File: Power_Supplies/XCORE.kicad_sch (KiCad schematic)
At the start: 11 parts, among them J22 FTSH-110-01-F-DV-K XTAG HEADER, U10 XU316-1024-TQ128-I24, U11 W25Q64JVSSIQ (FLASH MEMORY), X1 FA-238 24.0000MB-C0 (CRYSTAL)

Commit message: Added 3.3V/1.8V LDO, clock IC
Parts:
- removed C196, C197: 100N, Capacitor_SMD:C_0402_1005Metric, symbol Device:C
- removed J22: FTSH-110-01-F-DV-K XTAG HEADER, CON20_2X10_DUK_FTSH_SAI, symbol SDLibrary:FTSH-110-01-F-DV-K
- removed R174: 0, symbol Device:R
- added R45: 33, Resistor_SMD:R_0805_2012Metric, symbol Device:R
- added U31: Si5351A-B-GT, Package_SO:MSOP-10_3x3mm_P0.5mm, symbol Oscillator:Si5351A-B-GT
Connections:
- net 3.3V: now also U31.1 (VDD), U31.7 (VDDO); no longer U10.61 (USB_VDD33)
- net AGND: now also U31.8 (GND)
- removed net 0.9V: U10.14 (VDD), U10.41 (PLL_AVDD), U10.5 (VDD)
- removed net 1.8V: U10.35 (VDDIOB18), U10.56 (VDDIOB18), U10.62 (USB_VDD18)
- net XIN: no longer names the net of C100.2, R28.1, U10.34 (XIN)
- net XIN: no longer X1.1
- net XOUT: no longer names the net of C101.1, R28.2, U10.33 (XOUT)
- net XOUT: no longer X1.3
- new net: R45.1, U31.10 (CLK0)
- new net: U31.2 (XA), X1.1
- new net: U31.3 (XB), X1.3
- new net BCK: U31.6 (CLK2)
- new net LRCK: U31.9 (CLK1)
- new net MCLK: R45.2
- new net SCL: U31.4 (SCL)
- new net SDA: U31.5 (SDA)
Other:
- note added: "Device address = 0x60"
- note removed: "What are these for? (The XLs)"
- company: Joshua Yu -> Michael Meyers
- moved on the sheet: C100, C101, R28, R29, U10A, U10B, U11

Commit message: big things are coming...
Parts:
- X1: footprint FA-238_EPS -> SamacSys_Parts:FA-238_EPS
- renumbered C100 to C49, C101 to C50, R29 to R34, R45 to R35, R28 to R36, U10 to U12, U31 to U13, U11 to U14
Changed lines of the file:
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@@
 		(dnp no)
 		(fields_autoplaced yes)
-		(property "Reference" "C100"
+		(property "Reference" "C49"
 			(at 132.08 135.8899 0)
 			(effects
@@
 			(project ""
 				(path "/5266cf9e-da90-4c53-80fd-cf3dbed42632/4ac374da-48c1-45fc-82eb-58af98bfd6f4"
-					(reference "C100")
+					(reference "C49")
 					(unit 1)
 				)
@@
 		(dnp no)
 		(fields_autoplaced yes)
-		(property "Reference" "#PWR062"
+		(property "Reference" "#PWR047"
 			(at 76.2 175.26 0)
 			(effects
@@
 			(project "Power_Supplies"
 				(path "/5266cf9e-da90-4c53-80fd-cf3dbed42632/4ac374da-48c1-45fc-82eb-58af98bfd6f4"
-					(reference "#PWR062")
+					(reference "#PWR047")
 					(unit 1)
 				)
@@
 		(dnp no)
 		(fields_autoplaced yes)
-		(property "Reference" "#PWR0101"
+		(property "Reference" "#PWR049"
 			(at 114.3 48.26 0)
 			(effects
@@
 			(project "Power_Supplies"
 				(path "/5266cf9e-da90-4c53-80fd-cf3dbed42632/4ac374da-48c1-45fc-82eb-58af98bfd6f4"
-					(reference "#PWR0101")
+					(reference "#PWR049")
 					(unit 1)
 				)
@@
 		(dnp no)
 		(fields_autoplaced yes)
-		(property "Reference" "U10"
+		(property "Reference" "U12"
 			(at 217.17 52.07 0)
 			(effects
@@
 			(project ""
 				(path "/5266cf9e-da90-4c53-80fd-cf3dbed42632/4ac374da-48c1-45fc-82eb-58af98bfd6f4"
-					(reference "U10")
+					(reference "U12")
 					(unit 2)
 				)
@@
 		(dnp no)
 		(fields_autoplaced yes)
-		(property "Reference" "R29"
+		(property "Reference" "R34"
 			(at 102.87 17.78 90)
 			(effects
@@
 			(project ""
 				(path "/5266cf9e-da90-4c53-80fd-cf3dbed42632/4ac374da-48c1-45fc-82eb-58af98bfd6f4"
-					(reference "R29")
+					(reference "R34")
 					(unit 1)
 				)
@@
 		(dnp no)
 		(fields_autoplaced yes)
-		(property "Reference" "U31"
+		(property "Reference" "U13"
 			(at 101.2541 184.15 0)
 			(effects
@@
 			(project "Power_Supplies"
 				(path "/5266cf9e-da90-4c53-80fd-cf3dbed42632/4ac374da-48c1-45fc-82eb-58af98bfd6f4"
-					(reference "U31")
+					(reference "U13")
 					(unit 1)
 				)
@@
 		(dnp no)
 		(fields_autoplaced yes)
-		(property "Reference" "U11"
+		(property "Reference" "U14"
 			(at 154.94 21.59 0)
 			(effects
@@
 			(project ""
 				(path "/5266cf9e-da90-4c53-80fd-cf3dbed42632/4ac374da-48c1-45fc-82eb-58af98bfd6f4"
-					(reference "U11")
+					(reference "U14")
 					(unit 1)
 				)
@@
 		(dnp no)
 		(fields_autoplaced yes)
-		(property "Reference" "#PWR061"
+		(property "Reference" "#PWR046"
 			(at 41.91 177.8 0)
 			(effects
@@
 			(project "Power_Supplies"
 				(path "/5266cf9e-da90-4c53-80fd-cf3dbed42632/4ac374da-48c1-45fc-82eb-58af98bfd6f4"
-					(reference "#PWR061")
+					(reference "#PWR046")
 					(unit 1)
 				)
@@
 		(dnp no)
 		(fields_autoplaced yes)
-		(property "Reference" "U10"
+		(property "Reference" "U12"
 			(at 88.9 52.07 0)
 			(effects
@@
 			(project ""
 				(path "/5266cf9e-da90-4c53-80fd-cf3dbed42632/4ac374da-48c1-45fc-82eb-58af98bfd6f4"
-					(reference "U10")
+					(reference "U12")
 					(unit 1)
 				)
@@
 		(dnp no)
 		(fields_autoplaced yes)
-		(property "Reference" "#PWR0103"
+		(property "Reference" "#PWR048"
 			(at 99.06 190.5 0)
 			(effects
@@
 			(project "Power_Supplies"
 				(path "/5266cf9e-da90-4c53-80fd-cf3dbed42632/4ac374da-48c1-45fc-82eb-58af98bfd6f4"
-					(reference "#PWR0103")
+					(reference "#PWR048")
 					(unit 1)
 				)
@@
 		(dnp no)
 		(fields_autoplaced yes)
-		(property "Reference" "R45"
+		(property "Reference" "R35"
 			(at 118.11 160.02 90)
 			(effects
@@
 			(project "Power_Supplies"
 				(path "/5266cf9e-da90-4c53-80fd-cf3dbed42632/4ac374da-48c1-45fc-82eb-58af98bfd6f4"
-					(reference "R45")
+					(reference "R35")
 					(unit 1)
 				)
@@
 		(dnp no)
 		(fields_autoplaced yes)
-		(property "Reference" "#PWR0105"
+		(property "Reference" "#PWR050"
 			(at 128.27 127 0)
 			(effects
@@
 			(project ""
 				(path "/5266cf9e-da90-4c53-80fd-cf3dbed42632/4ac374da-48c1-45fc-82eb-58af98bfd6f4"
-					(reference "#PWR0105")
+					(reference "#PWR050")
 					(unit 1)
 				)
@@
 		(dnp no)
 		(fields_autoplaced yes)
-		(property "Reference" "R28"
+		(property "Reference" "R36"
 			(at 128.27 144.7799 0)
 			(effects
@@
 			(project ""
 				(path "/5266cf9e-da90-4c53-80fd-cf3dbed42632/4ac374da-48c1-45fc-82eb-58af98bfd6f4"
-					(reference "R28")
+					(reference "R36")
 					(unit 1)
 				)
@@
 			)
 		)
-		(property "Footprint" "FA-238_EPS"
+		(property "Footprint" "SamacSys_Parts:FA-238_EPS"
 			(at 46.99 167.64 0)
 			(effects
@@
 		(dnp no)
 		(fields_autoplaced yes)
-		(property "Reference" "#PWR0102"
+		(property "Reference" "#PWR051"
 			(at 165.1 165.1 0)
 			(effects
@@
 			(project "Power_Supplies"
 				(path "/5266cf9e-da90-4c53-80fd-cf3dbed42632/4ac374da-48c1-45fc-82eb-58af98bfd6f4"
-					(reference "#PWR0102")
+					(reference "#PWR051")
 					(unit 1)
 				)
@@
 		(dnp no)
 		(fields_autoplaced yes)
-		(property "Reference" "C101"
+		(property "Reference" "C50"
 			(at 168.91 153.6699 0)
 			(effects
@@
 			(project "Power_Supplies"
 				(path "/5266cf9e-da90-4c53-80fd-cf3dbed42632/4ac374da-48c1-45fc-82eb-58af98bfd6f4"
-					(reference "C101")
+					(reference "C50")
 					(unit 1)
 				)

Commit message: More XCORE PCB updates
Finished XTAG header, reinstated clock, worked on power pins
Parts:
- added C202, C203, C204, C205, C207, C208, C209, C210, C211, C212, C213, C214, C215, C216, C217, C218: 100nF, Capacitor_SMD:C_0402_1005Metric, symbol Device:C
- added C206: 2.2uF, Capacitor_SMD:C_0402_1005Metric, symbol Device:C
- added J8: FTSH-110-01-F-DV-K, CON20_2X10_DUK_FTSH_SAI, symbol SDLibrary:FTSH-110-01-F-DV-K
- added R164: 0, Resistor_SMD:R_0805_2012Metric, symbol Device:R
- added R165, R166: 43, Resistor_SMD:R_0805_2012Metric, symbol Device:R
- added X2: FA-238 24.0000MB-C0, FA-238_EPS, symbol SDLibrary:FA-238_24.0000MB-C0
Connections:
- net 3.3V: now also C203.1, J8.11
- net AGND: now also U12.129 (GND), U12.30 (GND), C202.2, C203.2, C204.2, C205.2, C206.2, C207.2, C208.2, C209.2, C210.2, C211.2, C212.2, C213.2, C214.2, C215.2, C216.2, C217.2, C218.2, J8.13, J8.15, J8.17, J8.19, J8.3, J8.5, J8.7, J8.9, X2.2, X2.4
- net XIN: now reaches C49.2, R36.1, U12.34 (XIN)
- net XIN: now also X2.1
- net 0.9V: now reaches U12.104 (VDD)
- net 0.9V: now also U12.105 (VDD), U12.106 (VDD), U12.11 (VDD), U12.113 (VDD), U12.14 (VDD), U12.18 (VDD), U12.39 (VDD), U12.41 (PLL_AVDD), U12.45 (VDD), U12.5 (VDD), U12.50 (VDD), U12.54 (VDD), U12.68 (VDD), U12.85 (VDD), U12.95 (VDD), C206.1, C207.1, C208.1, C209.1, C210.1, C211.1, C212.1, C213.1, C214.1, C215.1, C216.1, C217.1, C218.1
- net XL_DN1: now reaches U12.66 (X1D16)
- net XL_DN1: now also J8.12
- net XL_DN0: now reaches U12.67 (X1D17)
- net XL_DN0: now also J8.14
- net XL_UP0: now reaches U12.69 (X1D18)
- net XL_UP0: now also R166.1
- net XL_UP1: now reaches U12.70 (X1D19)
- net XL_UP1: now also R165.1
- net XOUT: now reaches C50.1, R36.2, U12.33 (XOUT)
- net XOUT: now also X2.3
- net TDI: now reaches U12.36 (TDI)
- net TDI: now also J8.8
- net TDO: now reaches U12.37 (TDO)
- net TDO: now also R164.1
- net TMS: now reaches U12.44 (TMS)
- net TMS: now also J8.2
- net TCK: now reaches U12.51 (TCK)
- net TCK: now also J8.4
- net 3.3V_LDO: now reaches U12.61 (USB_VDD33)
- net 3.3V_LDO: now also C205.1
- net 1.8V_LDO: now reaches U12.62 (USB_VDD18)
- net 1.8V_LDO: now also C204.1
- new net: J8.16, R166.2
- new net: J8.18, R165.2
- new net: J8.6, R164.2
- new net 1.8V: C202.1, J8.1
- new net RST_N: J8.10
- no-connect marks 0 -> 9
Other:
- note added: "Place 100nF bypass caps as close as possible to supply"
- moved on the sheet: C49, C50, R34, R35, R36, U12A, U12B, U13, U14, X1

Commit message: More PCB work
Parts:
- added C232: 1uF, Capacitor_SMD:C_0402_1005Metric, symbol Device:C
- added FL1: BLM18AG601SZ1D, BLM18AG601SZ1D:BEADC1608X95N, symbol SDLibrary:BLM18AG601SZ1D
- added J22: 2171790001, 2171790001_MOL, symbol SDLibrary:2171790001
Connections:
- net 0.9V: now also FL1.2; no longer U12.41 (PLL_AVDD)
- net 1.8V_LDO: now also U12.10 (VDDIOL), U12.109 (VDDIOT), U12.121 (VDDIOT), U12.17 (VDDIOL), U12.35 (VDDIOB18), U12.56 (VDDIOB18), U12.72 (VDDIOR), U12.89 (VDDIOR)
- net AGND: now also U12.24 (MIPI_VDD18), U12.27 (MIPI_VDD09), U12.40 (LV_L_N), U12.42 (PLL_AGND), U12.43 (LV_T_N), U12.52 (LV_R_N), C232.2, J22.A1/B12 (GND), J22.B1/A12 (GND)
- net RST_N: now also U12.38 (RST_N)
- net USB_DN: now reaches U12.59 (USB_DM)
- net USB_DN: now also J22.A7 (DN1)
- net USB_DP: now reaches U12.60 (USB_DP)
- net USB_DP: now also J22.A6 (DP1)
- new net: C232.1, FL1.1, U12.41 (PLL_AVDD)
- no-connect marks 9 -> 3
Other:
- note added: "Ferrite bead for filtering"
- note added: "Place low inductance MLCC 100nF bypass caps as close as possible to supply"
- note removed: "Place 100nF bypass caps as close as possible to supply"
- moved on the sheet: C204, C205, C206, C207, C208, C209, C210, C211, C212, C213, C214, C215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

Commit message: initial placement of all cmponents
need to add:
- pin headers for Rpi
- separate the boards and add pin headers for connection points
- probably get rid of buck converters and change LDOs to be higher current
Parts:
- FL1: footprint BLM18AG601SZ1D:BEADC1608X95N -> SamacSys_Parts:BLM18SP221SN1B
- J22: footprint 2171790001_MOL -> Connector_Molex:Molex_Micro-Fit_3.0_43045-1615_2x08_P3.00mm_Vertical
- J8: footprint CON20_2X10_DUK_FTSH_SAI -> SamacSys_Parts:FTSH-110-XX-YYY-DV-K-A
- X2: footprint FA-238_EPS -> SamacSys_Parts:FA-238_EPS
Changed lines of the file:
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@@
 			)
 		)
-		(property "Footprint" "2171790001_MOL"
+		(property "Footprint" "Connector_Molex:Molex_Micro-Fit_3.0_43045-1615_2x08_P3.00mm_Vertical"
 			(at 266.7 77.47 0)
 			(effects
@@
 			)
 		)
-		(property "Footprint" "CON20_2X10_DUK_FTSH_SAI"
+		(property "Footprint" "SamacSys_Parts:FTSH-110-XX-YYY-DV-K-A"
 			(at 132.08 60.96 0)
 			(effects
@@
 			)
 		)
-		(property "Footprint" "FA-238_EPS"
+		(property "Footprint" "SamacSys_Parts:FA-238_EPS"
 			(at 295.91 347.98 0)
 			(effects
@@
 			)
 		)
-		(property "Footprint" "BLM18AG601SZ1D:BEADC1608X95N"
+		(property "Footprint" "SamacSys_Parts:BLM18SP221SN1B"
 			(at 260.35 225.298 0)
 			(effects

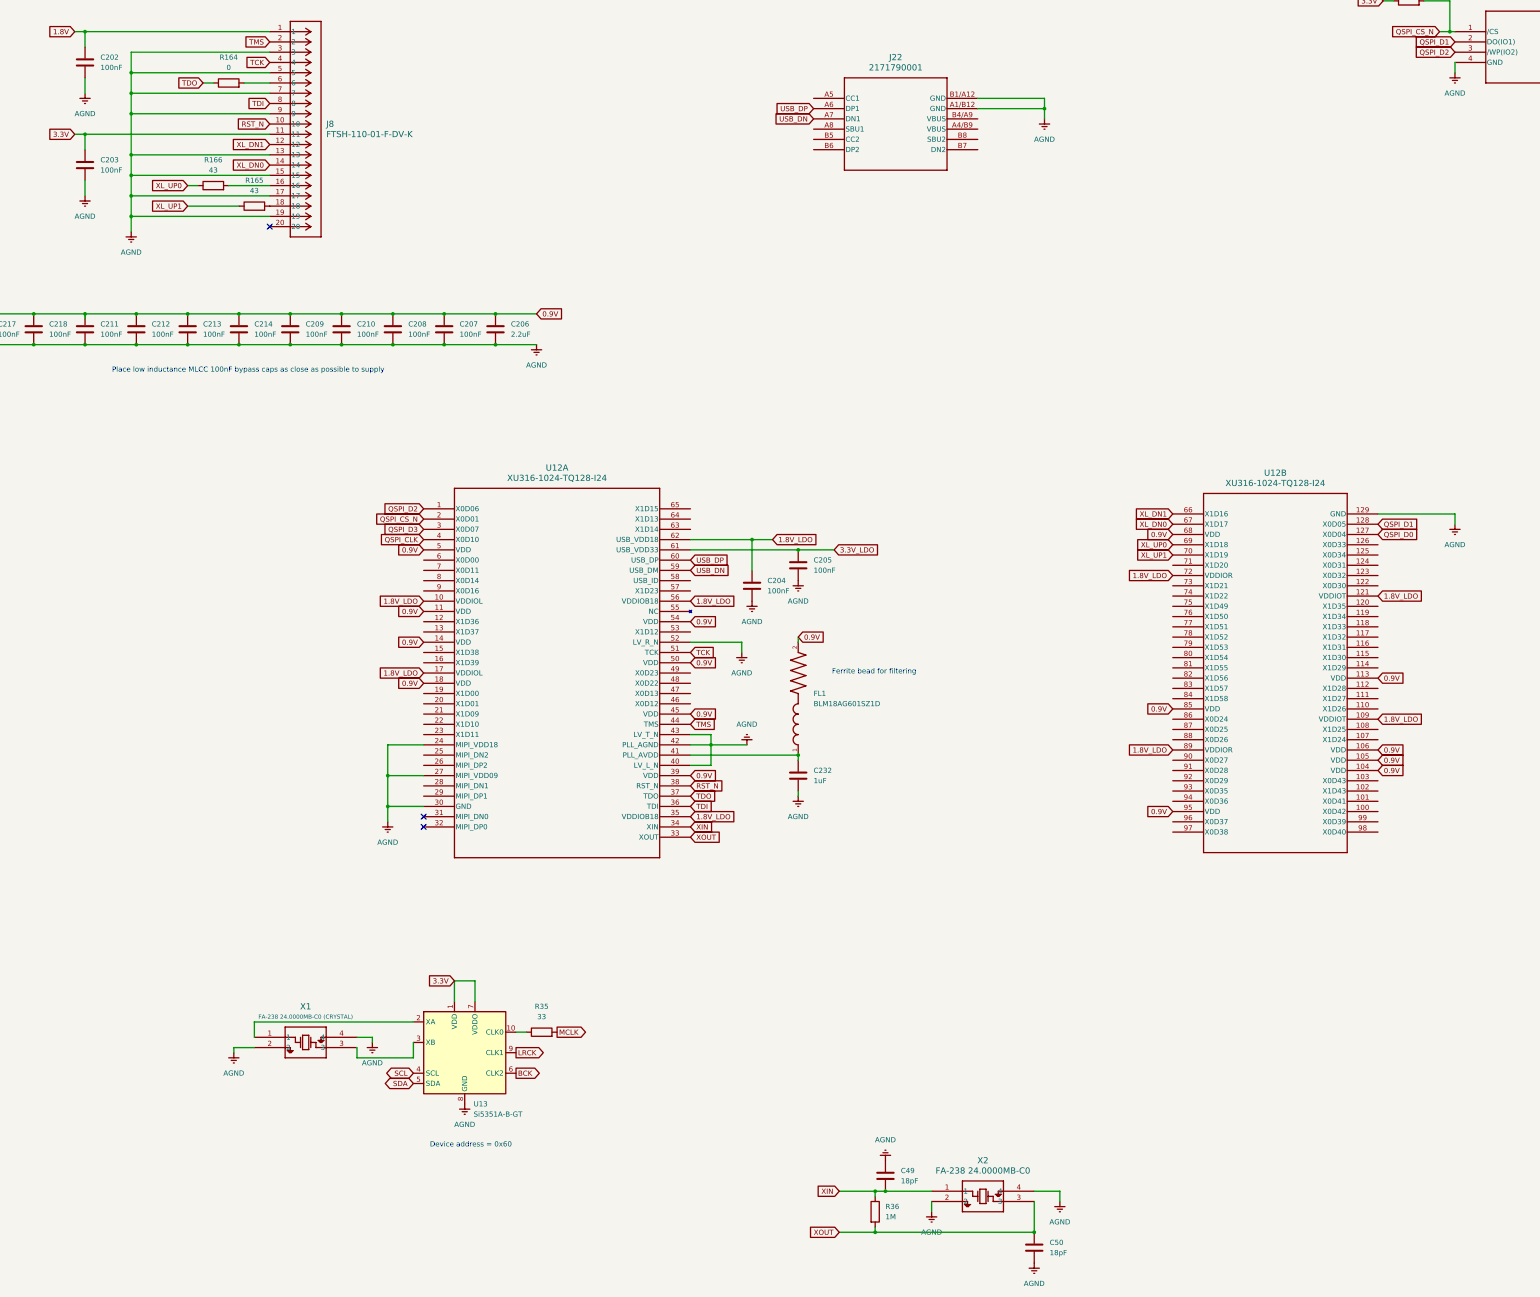
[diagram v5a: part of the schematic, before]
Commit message: Added stuff for the power supply circuitry
changed all grounds to GND (same ground plane)
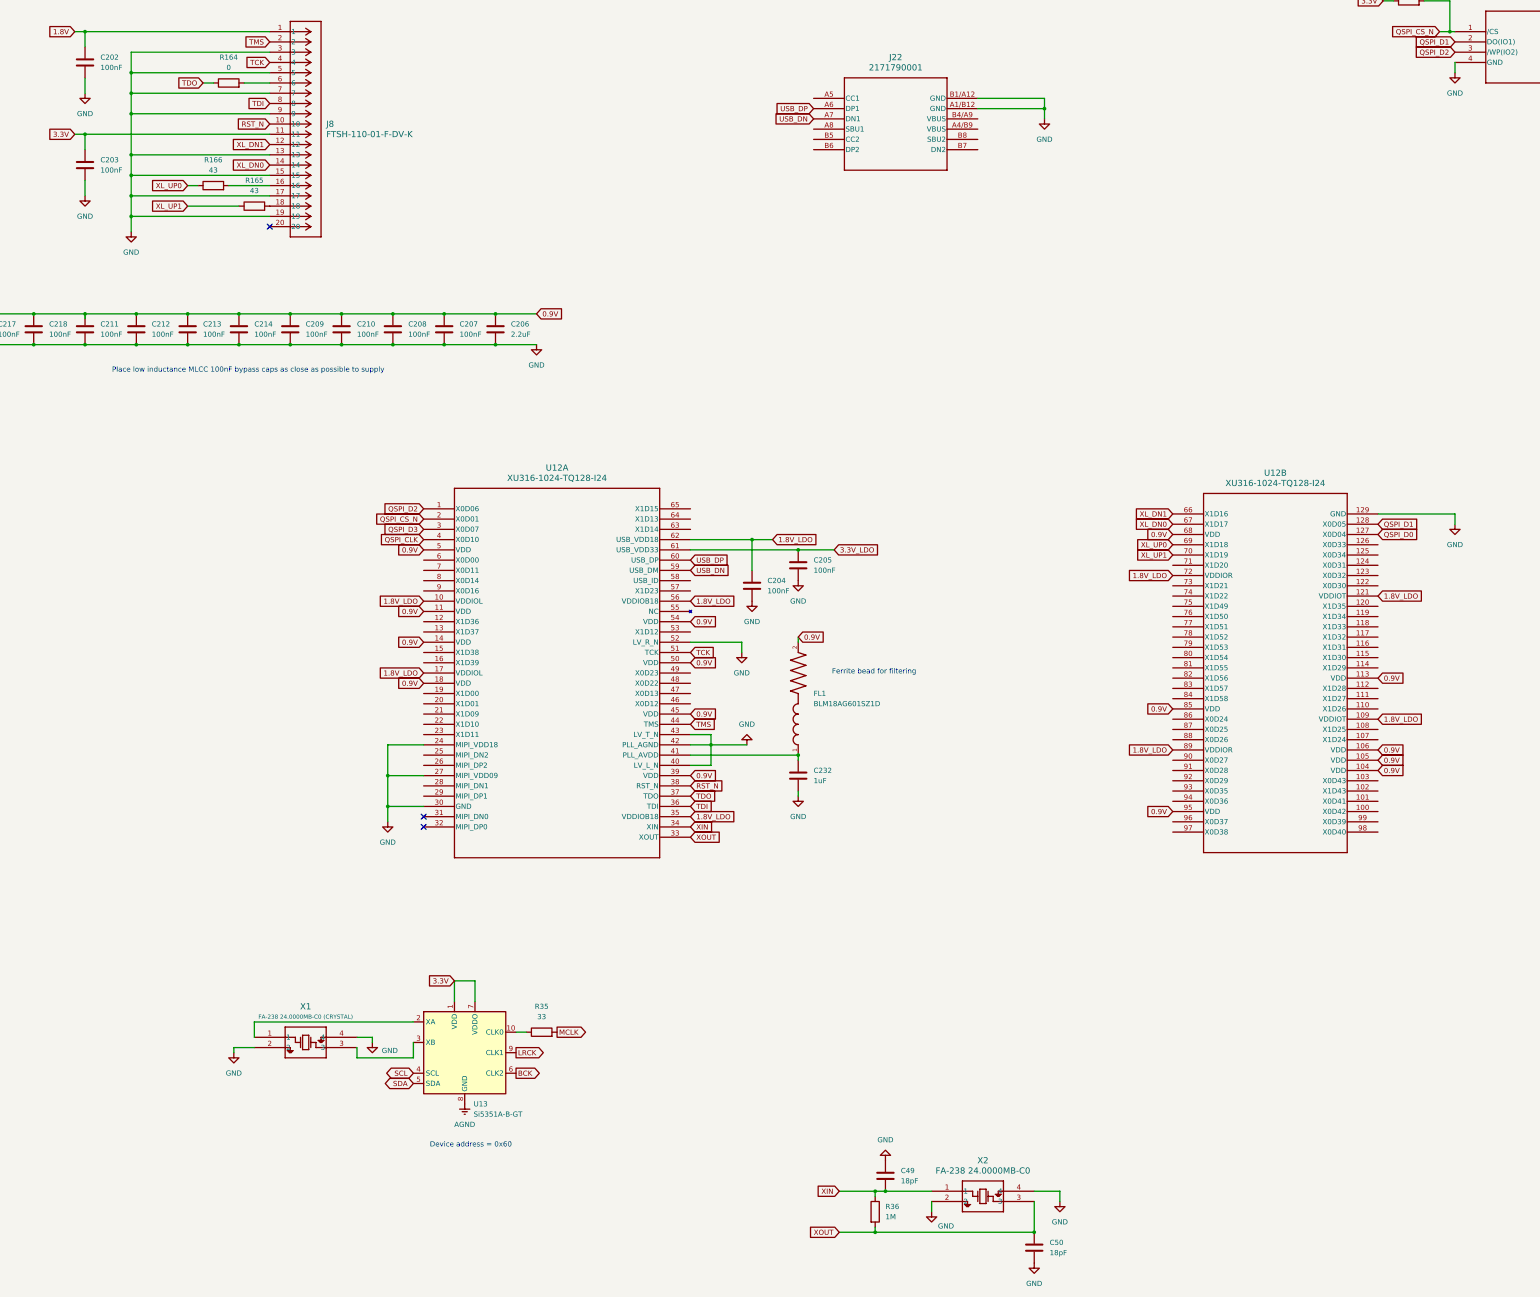
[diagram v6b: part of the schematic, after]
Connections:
- net AGND: no longer C202.2, C203.2, C204.2, C205.2, C206.2, C207.2, C208.2, C209.2, C210.2, C211.2, C212.2, C213.2, C214.2, C215.2, C216.2, C217.2, C218.2, C232.2, C49.1, C50.2, J22.A1/B12 (GND), J22.B1/A12 (GND), J8.13, J8.15, J8.17, J8.19, J8.3, J8.5, J8.7, J8.9, U12.129 (GND), U12.24 (MIPI_VDD18), U12.27 (MIPI_VDD09), U12.30 (GND), U12.40 (LV_L_N), U12.42 (PLL_AGND), U12.43 (LV_T_N), U12.52 (LV_R_N), U14.4 (GND), X1.2, X1.4, X2.2, X2.4
- new net GND: C202.2, C203.2, C204.2, C205.2, C206.2, C207.2, C208.2, C209.2, C210.2, C211.2, C212.2, C213.2, C214.2, C215.2, C216.2, C217.2, C218.2, C232.2, C49.1, C50.2, J22.A1/B12 (GND), J22.B1/A12 (GND), J8.13, J8.15, J8.17, J8.19, J8.3, J8.5, J8.7, J8.9, U12.129 (GND), U12.24 (MIPI_VDD18), U12.27 (MIPI_VDD09), U12.30 (GND), U12.40 (LV_L_N), U12.42 (PLL_AGND), U12.43 (LV_T_N), U12.52 (LV_R_N), U14.4 (GND), X1.2, X1.4, X2.2, X2.4
